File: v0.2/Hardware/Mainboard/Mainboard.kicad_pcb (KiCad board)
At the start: 2 copper layers, 44 x 44 mm, 16 parts

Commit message: v0.2: Finished schematics
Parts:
- removed the REF** at (149.9, 81.6)
- removed the REF** at (131.8, 79.8)
- removed the REF** at (131.8, 107.0)
- removed the REF** at (133.1, 114.5)
- removed the REF** at (140.8, 114.5)
- removed the REF** at (148.4, 114.5)
- removed the REF** at (166.0, 90.0)
- removed the REF** at (170.5, 97.0)
- removed the REF** at (129.5, 90.0)
- removed the REF** at (163.0, 83.0)
- removed the REF** at (137.0, 108.0)
- removed the REF** at (168.2, 107.0)
- removed the REF** at (168.2, 79.8)
- added REF**: PinHeader_1x05_P2.54mm_Vertical, Connector_PinHeader_2.54mm:PinHeader_1x05_P2.54mm_Vertical, B.Cu at (0.10, -19.5)
- added REF**: MountingHole_2.7mm_M2.5, MountingHole:MountingHole_2.7mm_M2.5, F.Cu at (-18.2, -18.2)
- added REF**: MountingHole_2.7mm_M2.5, MountingHole:MountingHole_2.7mm_M2.5, F.Cu at (-18.2, 9.00)
- added REF**: WJ124-3.81-2P, _AKL_Connector:WJ124-3.81-2P, B.Cu at (-16.9, 16.5)
- added REF**: WJ124-3.81-2P, _AKL_Connector:WJ124-3.81-2P, B.Cu at (-9.24, 16.5)
- added REF**: WJ124-3.81-2P, _AKL_Connector:WJ124-3.81-2P, B.Cu at (-1.62, 16.5)
- added REF**: MLT-7525, _AKL_Speaker:MLT-7525, B.Cu at (-10.0, -16.8)
- added REF**: SSD1306_0.96_128x64_I2C, _AKL_Display:SSD1306_0.96_128x64_I2C, F.Cu at (0.00, -2.62)
- added REF**: SW_PUSH_6mm_H8mm, Button_Switch_THT:SW_PUSH_6mm_H8mm, F.Cu at (16.0, -6.00)
- added REF**: SW_PUSH_6mm_H8mm, Button_Switch_THT:SW_PUSH_6mm_H8mm, F.Cu at (20.5, -3.00)
- added REF**: SW_PUSH_6mm_H8mm, Button_Switch_THT:SW_PUSH_6mm_H8mm, F.Cu at (-20.5, -6.00)
- added REF**: MountingHole_2.7mm_M2.5, MountingHole:MountingHole_2.7mm_M2.5, F.Cu at (18.2, 9.00)
- added REF**: MountingHole_2.7mm_M2.5, MountingHole:MountingHole_2.7mm_M2.5, F.Cu at (18.2, -18.2)
- moved REF** 180.3 mm to (-16.0, -3.00)
- moved REF** 179.2 mm to (6.00, 16.5)
- moved REF** 179.2 mm to (16.0, 18.5)
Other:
- board text added: "42x68mm?"

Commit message: v0.2: Preliminary placement
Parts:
- removed the REF** at (0.10, -19.5)
- removed the REF** at (-16.9, 16.5)
- removed the REF** at (-9.24, 16.5)
- removed the REF** at (-1.62, 16.5)
- removed the REF** at (6.00, 16.5)
- removed the REF** at (16.0, 18.5)
- removed the REF** at (-10.0, -16.8)
- removed the REF** at (0.00, -2.62)
- removed the REF** at (16.0, -6.00)
- removed the REF** at (20.5, -3.00)
- removed the REF** at (-20.5, -6.00)
- removed the REF** at (-16.0, -3.00)
- added BZ1: MLT-7525, _AKL_Speaker:MLT-7525, B.Cu at (-10.3, -17.6)
- added C1: 10u, Capacitor_SMD:C_0603_1608Metric, B.Cu at (11.0, 0.00)
- added C2: 10u, Capacitor_SMD:C_0603_1608Metric, B.Cu at (11.0, -6.00)
- added C3: 10u, Capacitor_SMD:C_0603_1608Metric, B.Cu at (2.00, -11.0)
- added C4: 100n, Capacitor_SMD:C_0603_1608Metric, B.Cu at (2.00, -9.00)
- added C5: 10n, Capacitor_SMD:C_0603_1608Metric, B.Cu at (-1.62, 11.8)
- added C6: 100n, Capacitor_SMD:C_0603_1608Metric, B.Cu at (14.7, 6.30)
- added C7: 100n, Capacitor_SMD:C_0603_1608Metric, B.Cu at (-5.30, 10.2)
- added D1: MBR120VLSFT3G, _AKL_Diode:SOD-123FL, B.Cu at (4.90, 10.2)
- added D2: MBR120VLSFT3G, _AKL_Diode:SOD-123FL, B.Cu at (7.10, 10.2)
- added D3: MBR120VLSFT3G, _AKL_Diode:SOD-123FL, B.Cu at (-8.10, 2.80)
- added D4: MBR120VLSFT3G, _AKL_Diode:SOD-123FL, B.Cu at (-12.6, 2.80)
- added D5: MBR120VLSFT3G, _AKL_Diode:SOD-123FL, B.Cu at (-12.1, -12.5)
- added DS1: SSD1306_0.96_128x64_I2C, _AKL_Display:SSD1306_0.96_128x64_I2C, F.Cu at (0.00, -2.62)
- added J1: 5V, _AKL_Connector:WJ124-3.81-2P, B.Cu at (6.00, 16.7)
- added J2: TYPE-C-31-M-12, Connector_USB:USB_C_Receptacle_HRO_TYPE-C-31-M-12, B.Cu at (16.0, 18.6)
- added J3: Debug, Connector_PinHeader_2.54mm:PinHeader_1x05_P2.54mm_Vertical, B.Cu at (3.00, -20.0)
- added J4: TC, _AKL_Connector:WJ124-3.81-2P, B.Cu at (-1.62, 16.7)
- added J5: S1, _AKL_Connector:WJ124-3.81-2P, B.Cu at (-9.24, 16.7)
- added J6: S2, _AKL_Connector:WJ124-3.81-2P, B.Cu at (-16.9, 16.7)
- added Q1: BSS138P, Package_TO_SOT_SMD:SOT-23, B.Cu at (-7.70, -4.30)
- added Q2: BSS138P, Package_TO_SOT_SMD:SOT-23, B.Cu at (-11.7, -4.30)
- added Q3: BSS138P, Package_TO_SOT_SMD:SOT-23, B.Cu at (-7.80, -11.6)
- added R1: 5K1, Resistor_SMD:R_0603_1608Metric, B.Cu at (-17.0, -10.3)
- added R10: DNP, Resistor_SMD:R_0603_1608Metric, B.Cu at (8.18, 2.19)
- added R11: DNP, Resistor_SMD:R_0603_1608Metric, B.Cu at (8.00, 4.00)
- added R12: 5K1, Resistor_SMD:R_0603_1608Metric, B.Cu at (-7.70, -6.80)
- added R13: 5K1, Resistor_SMD:R_0603_1608Metric, B.Cu at (-11.7, -6.80)
- added R14: 5K1, Resistor_SMD:R_0603_1608Metric, B.Cu at (-4.80, -11.6)
- added R15: 100, Resistor_SMD:R_0603_1608Metric, B.Cu at (-12.4, -10.6)
- added R2: 5K1, Resistor_SMD:R_0603_1608Metric, B.Cu at (-17.0, -0.80)
- added R3: DNP, Resistor_SMD:R_0603_1608Metric, B.Cu at (-2.00, -18.0)
- added R4: 5K1, Resistor_SMD:R_0603_1608Metric, B.Cu at (17.0, -10.3)
- added R5: 5K1, Resistor_SMD:R_0603_1608Metric, B.Cu at (11.4, 12.5)
- added R6: DNP, Resistor_SMD:R_0603_1608Metric, B.Cu at (0.00, -18.0)
- added R7: 5K1, Resistor_SMD:R_0603_1608Metric, B.Cu at (19.8, 12.7)
- added R8: 5K1, Resistor_SMD:R_0603_1608Metric, B.Cu at (17.0, -0.80)
- added R9: 5K1, Resistor_SMD:R_0603_1608Metric, B.Cu at (5.00, -9.00)
- added SW1: UP, Button_Switch_THT:SW_PUSH_6mm_H9.5mm, F.Cu at (-16.0, -12.5)
- added SW2: DOWN, Button_Switch_THT:SW_PUSH_6mm_H9.5mm, F.Cu at (-16.0, -3.00)
- added SW3: OK, Button_Switch_THT:SW_PUSH_6mm_H9.5mm, F.Cu at (16.0, -6.00)
- added SW4: BACK, Button_Switch_THT:SW_PUSH_6mm_H9.5mm, F.Cu at (16.0, 3.50)
- added TP1: 3V3, TestPoint:TestPoint_Pad_D2.0mm, F.Cu at (25.5, -0.30)
- added TP2: TXD, TestPoint:TestPoint_Pad_D2.0mm, F.Cu at (35.9, -3.40)
- added TP3: RXD, TestPoint:TestPoint_Pad_D2.0mm, F.Cu at (28.6, -0.40)
- added TP4: SCK, TestPoint:TestPoint_Pad_D2.0mm, F.Cu at (25.4, -3.80)
- added TP5: MISO, TestPoint:TestPoint_Pad_D2.0mm, F.Cu at (28.7, -3.80)
- added TP6: SCL, TestPoint:TestPoint_Pad_D2.0mm, F.Cu at (32.0, -3.70)
- added TP7: SDA, TestPoint:TestPoint_Pad_D2.0mm, F.Cu at (32.1, -0.10)
- added U1: AP7333-33SAG-7, Package_TO_SOT_SMD:SOT-23, B.Cu at (11.0, -3.00)
- added U2: CH340E, Package_SO:MSOP-10_3x3mm_P0.5mm, B.Cu at (12.0, 8.00)
- added U3: STM32G030K6T6, Package_QFP:LQFP-32_7x7mm_P0.8mm, B.Cu at (2.00, -3.00)
- added U4: MAX31855KASA+T, Package_SO:SOIC-8_3.9x4.9mm_P1.27mm, B.Cu at (-1.62, 7.10)
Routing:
- added copper zone on B.Cu, net GND
- added copper zone on F.Cu, net GND
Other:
- net class Default: trace_width 0.25 -> 0.2; via_dia 0.8 -> 0.7; via_drill 0.4 -> 0.3
- rule via_min_size: 0.4 -> 0.7
- board text added: "+"
- board text added: "-"
- board text added: "5V"
- board text added: "FAN"
- board text added: "SSR"
- board text added: "TC"
- board text removed: "+ 5V -"
- board text removed: "+ S1 -"
- board text removed: "+ S2 -"
- board text removed: "+ TC -"
- board text removed: "42x68mm?"

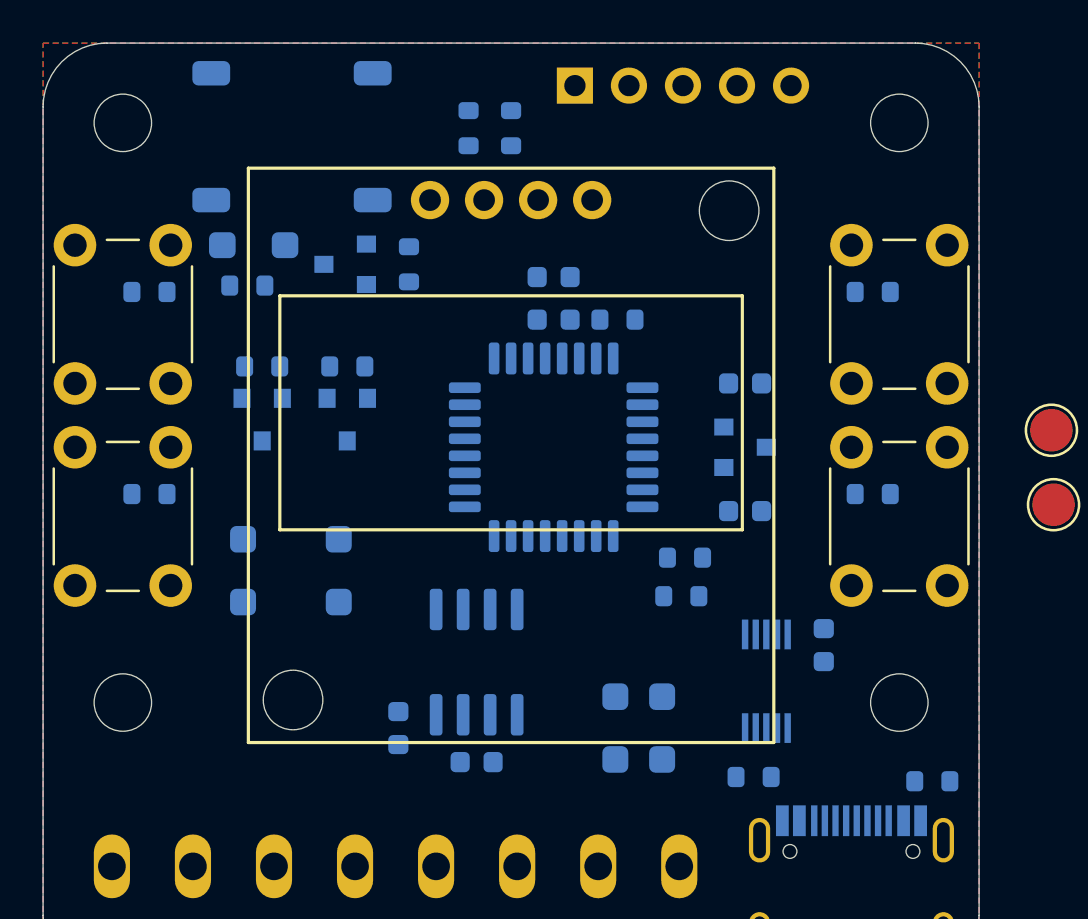
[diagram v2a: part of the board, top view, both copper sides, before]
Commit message: v0.2: Updated placement
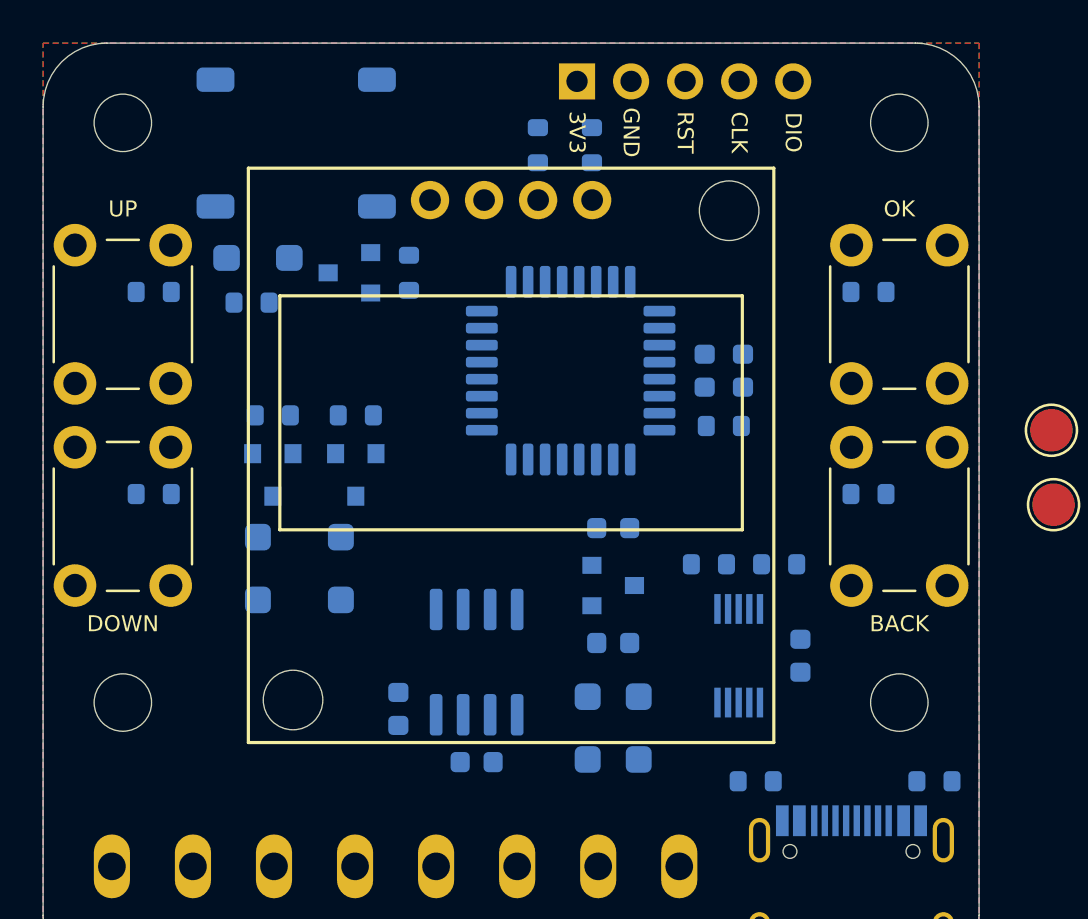
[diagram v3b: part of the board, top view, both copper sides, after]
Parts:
- moved C3 9.93 mm to (10.9, -6.60), turned to 90 degrees
- moved C2 9.20 mm to (4.80, 0.80)
- moved U1 8.98 mm to (4.80, 3.50)
- moved C1 8.77 mm to (4.80, 6.20)
- moved SW1 7.91 mm to (-20.5, -6.00), turned to 90 degrees
- moved SW4 7.91 mm to (20.5, -3.00), turned to 270 degrees
- moved C4 7.49 mm to (9.10, -6.60), turned to 270 degrees
- moved R9 7.07 mm to (10.0, -4.00)
- moved R10 4.44 mm to (12.6, 2.50), turned to 180 degrees
- moved R6 3.88 mm to (3.80, -17.2)
- moved U3 3.69 mm to (2.80, -6.60), turned to 180 degrees
- moved D2 3.50 mm to (3.60, 10.2)
- moved R3 3.36 mm to (1.26, -17.2)
- moved Q2 2.65 mm to (-11.2, -1.70)
- moved Q1 2.63 mm to (-7.30, -1.70)
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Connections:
- SW1 pad 1: /BTN_UP -> /3V3
- SW1 pad 2: /3V3 -> /BTN_UP
- SW4 pad 1: /BTN_BACK -> /3V3
- SW4 pad 2: /3V3 -> /BTN_BACK
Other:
- board text added: "3V3"
- board text added: "BACK"
- board text added: "CLK"
- board text added: "DIO"
- board text added: "DOWN"
- board text added: "GND"
- board text added: "OK"
- board text added: "RST"
- board text added: "UP"

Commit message: v0.2: Finished PCBs
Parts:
- removed TP1: 3V3, TestPoint:TestPoint_Pad_D2.0mm
- removed TP2: TXD, TestPoint:TestPoint_Pad_D2.0mm
- removed TP3: RXD, TestPoint:TestPoint_Pad_D2.0mm
- removed TP4: SCK, TestPoint:TestPoint_Pad_D2.0mm
- removed TP5: MISO, TestPoint:TestPoint_Pad_D2.0mm
- removed TP6: SCL, TestPoint:TestPoint_Pad_D2.0mm
- removed TP7: SDA, TestPoint:TestPoint_Pad_D2.0mm
- moved R5 2.30 mm to (9.40, 11.8)
- moved R15 1.34 mm to (-13.4, -9.20), turned to 90 degrees
- moved C7 1.05 mm to (-5.30, 10.3), turned to 270 degrees
- moved C1 0.25 mm to (4.55, 6.20)
- moved C2 0.25 mm to (4.55, 0.80)
- turned C3 to 270 degrees
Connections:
- U3 pad 1: (no net) -> /BTN_OK
- U3 pad 14: /BTN_OK -> (no net)
- U3 pad 18: /PWM_BUZZER -> (no net)
- U3 pad 26: (no net) -> /BTN_DOWN
- U3 pad 27: (no net) -> /BTN_UP
- U3 pad 28: (no net) -> /PWM_BUZZER
- U3 pad 7: /BTN_DOWN -> (no net)
- U3 pad 8: /BTN_UP -> (no net)
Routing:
- net /3V3: track 0.00 -> 164.0 mm, vias 0 -> 2
- net /5V: track 0.00 -> 83.5 mm, vias 0 -> 4
- net /BTN_BACK: track 0.00 -> 42.6 mm, vias 0 -> 1
- net /BTN_UP: track 0.00 -> 33.0 mm
- net /BTN_DOWN: track 0.00 -> 29.7 mm
- net /OUT_SSR-: track 0.00 -> 28.5 mm
- net /VUSB: track 0.00 -> 25.6 mm, vias 0 -> 4
- net /NRST: track 0.00 -> 22.9 mm, vias 0 -> 1
- net /SWDIO: track 0.00 -> 22.4 mm, vias 0 -> 1
- net GND: track 0.00 -> 21.5 mm, vias 0 -> 59
- net /MCU_TXD: track 0.00 -> 19.5 mm, vias 0 -> 2
- net /OUT_FAN-: track 0.00 -> 19.0 mm
- net /MCU_RXD: track 0.00 -> 18.9 mm, vias 0 -> 2
- net /BTN_OK: track 0.00 -> 16.8 mm, vias 0 -> 1
- net /OUT_FAN: track 0.00 -> 14.6 mm
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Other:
- net class 3V3 added: clearance 0.2, trace_width 0.5, via_dia 0.6, via_drill 0.3
- net class Default: via_dia 0.7 -> 0.6
- net class Power added: clearance 0.2, trace_width 0.5, via_dia 0.6, via_drill 0.3
- net class USB added: clearance 0.2, trace_width 0.2, via_dia 0.6, via_drill 0.3
- rule via_min_size: 0.7 -> 0.6
- board text added: "21/05 v0.2"
- board text added: "LUNAEmbedded.com"
- board text added: "Reflow Controller"
